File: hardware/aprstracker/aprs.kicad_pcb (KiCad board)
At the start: 2 copper layers, 125 parts, among them IC1 ATMEGA8-AI, J1 SMA, J2 SMA, P1 CONN_6, P3 CONN_2, Q1 MMBT5551, Q2 MMBT5551, Q3 BCX54, Q4 BFR93A, Q5 BFR93A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

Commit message: [HW] Add uncommited changes / PCB updates
Signed-off-by: Angel Hitov <angelhitov@gmail.com>
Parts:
- removed C20, C48: C, SM0805
- removed C36, C45, C47, C49: CAPAPOL, c_elec_6.3x4.5
- added ASTUB: VAL**, ASTUB, F.Cu at (164.7, 85.9)
- added D8: LED, LED-0805, F.Cu at (184.7, 90.3)
- added R30: R, SM0805, F.Cu at (188.1, 89.3)
- moved C43 77.2 mm to (109.0, 102.0), turned to 270 degrees
- moved R24 56.2 mm to (149.4, 94.2), turned to 270 degrees
- moved C1 53.8 mm to (133.7, 109.7)
- moved C50 53.1 mm to (184.8, 118.6), turned to 0 degrees
- moved C51 51.9 mm to (172.3, 116.2), turned to 0 degrees
- moved C22 50.5 mm to (153.0, 94.6), turned to 180 degrees
- moved C23 49.3 mm to (151.6, 86.7), turned to 180 degrees
- moved C18 48.8 mm to (157.6, 90.9), turned to 90 degrees
- moved D1 48.8 mm to (161.3, 100.2)
- moved C11 48.7 mm to (166.1, 111.9)
- moved C12 48.7 mm to (162.6, 111.9)
- moved C15 48.7 mm to (161.3, 97.5)
- moved C17 48.7 mm to (159.8, 90.9)
- moved C21 48.7 mm to (132.8, 95.2)
- moved C29 48.7 mm to (100.8, 105.7)
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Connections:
- C1 pad 2: N-0000089 (its old number) -> N-0000090
- C23 pad 1: N-0000060 (its old number) -> N-0000059
- C24 pad 1: N-0000060 (its old number) -> N-0000059
- C4 pad 2: N-0000022 -> N-0000019
- C5 pad 2: N-0000021 -> N-0000022
- IC1 pad 7: N-0000022 -> N-0000019
- IC1 pad 8: N-0000021 -> N-0000022
- L7 pad 2: N-0000060 (its old number) -> N-0000059
- Q5 pad 2: N-0000082 (its old number) -> N-0000043
- Q5 pad 3: N-0000060 (its old number) -> N-0000059
- R24 pad 1: N-0000082 (its old number) -> N-0000059
- R26 pad 1: N-0000082 (its old number) -> N-0000043
- U1 pad 2: N-0000089 (its old number) -> N-0000090
- X1 pad 1: N-0000089 (its old number) -> N-0000013
- X1 pad 2: N-0000013 -> N-0000090
- X2 pad 1: N-0000021 -> N-0000019
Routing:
- net VCC: track 0.00 -> 98.5 mm
- net TXD: track 0.00 -> 81.1 mm
- net RXD: track 0.00 -> 66.4 mm
- net N-0000034: track 0.00 -> 42.6 mm
- net N-0000068: track 0.00 -> 24.3 mm
- net N-0000094: track 0.00 -> 23.0 mm
- net RF_EN: track 0.00 -> 20.3 mm
- net N-0000011: track 0.00 -> 18.0 mm
- net N-0000022: track 0.00 -> 16.2 mm
- net N-0000019: track 0.00 -> 14.7 mm
- net N-0000059: track 0.00 -> 14.2 mm
- net N-0000025: track 0.00 -> 13.2 mm
- net N-0000044: track 0.00 -> 11.1 mm
- net N-0000027: track 0.00 -> 10.8 mm
- net N-0000024: track 0.00 -> 10.8 mm
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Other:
- board outline added: 102 x 38 mm

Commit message: [HW] route pcb
Signed-off-by: Angel Hitov <angelhitov@gmail.com>
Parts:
- moved R14 47.4 mm to (108.8, 96.9), turned to 90 degrees
- moved L16 46.8 mm to (162.7, 118.1)
- moved C32 12.3 mm to (121.3, 83.3), turned to 180 degrees
- moved D4 5.23 mm to (125.2, 102.6), turned to 0 degrees
- moved Q2 3.24 mm to (107.2, 92.6), turned to 90 degrees
- moved C38 2.17 mm to (116.8, 102.1)
- moved C21 1.48 mm to (133.6, 94.0), turned to 180 degrees
- moved R16 1.02 mm to (126.4, 110.9)
- moved L3 0.89 mm to (128.8, 107.1)
- moved R27 0.51 mm to (101.0, 99.3)
- moved Q7 0.51 mm to (101.0, 96.4)
- moved R29 0.38 mm to (101.3, 93.3)
- moved R28 0.25 mm to (98.2, 100.6)
- moved R9 0.25 mm to (152.7, 104.3)
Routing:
- net GND: track 6.69 -> 266.8 mm, vias 0 -> 70
- net VDD: track 7.79 -> 113.1 mm, vias 0 -> 3
- net +5V: track 6.26 -> 86.3 mm, vias 0 -> 1
- net DATA: track 0.00 -> 76.9 mm, vias 0 -> 1
- net CL: track 0.00 -> 72.5 mm, vias 0 -> 1
- net N-0000029: track 0.00 -> 72.2 mm, vias 0 -> 2
- net CE: track 0.00 -> 71.7 mm, vias 0 -> 2
- net RF_PWR: track 0.00 -> 67.4 mm, vias 0 -> 2
- net 3V3: track 0.00 -> 57.9 mm, vias 0 -> 2
- net N-0000094: track 23.0 -> 56.3 mm, vias 0 -> 3
- net N-000002: track 0.00 -> 22.4 mm
- net N-0000044: track 11.1 -> 31.3 mm, vias 0 -> 2
- net N-0000091: track 0.00 -> 20.0 mm
- net N-0000064: track 0.00 -> 18.8 mm
- net N-0000067: track 0.00 -> 14.7 mm
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- added copper zone on B.Cu, net GND
- added copper zone on F.Cu, net GND
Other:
- rule via_min_drill: 0.508 -> 0.4
- rule via_min_size: 0.889 -> 0.8

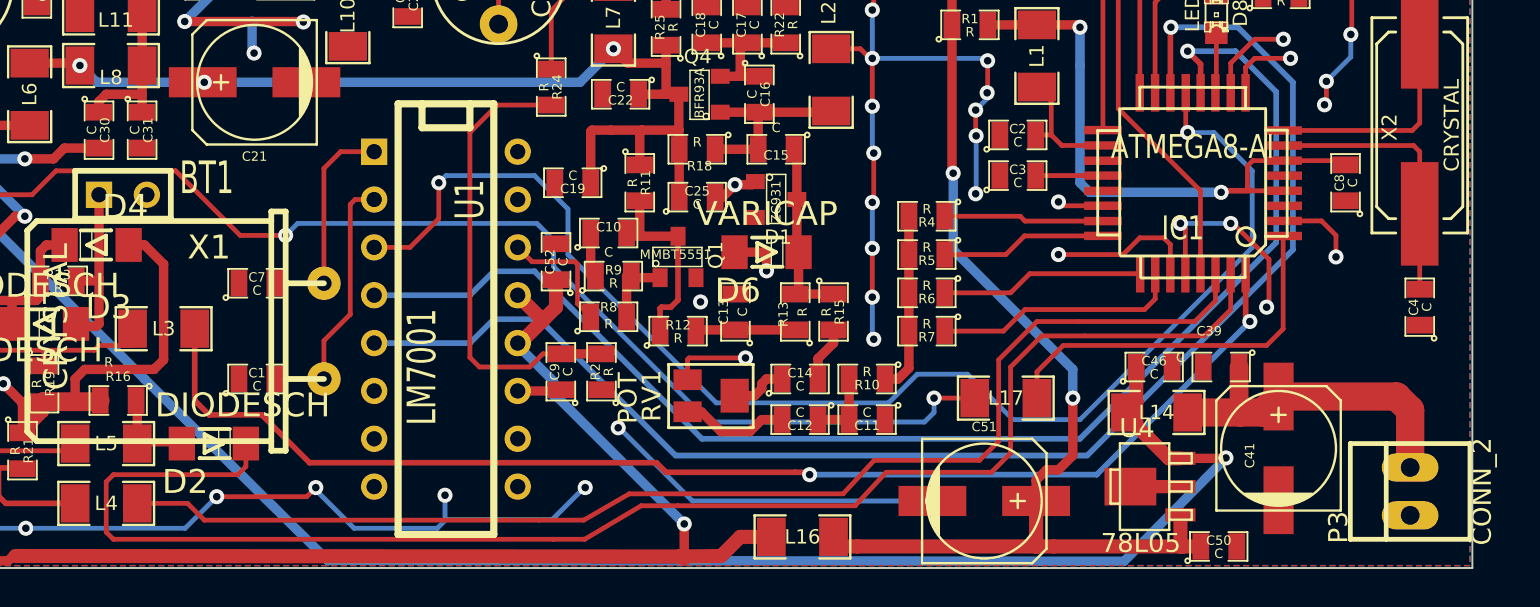
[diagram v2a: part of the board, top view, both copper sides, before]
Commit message: [HW] PCB Ground plane update
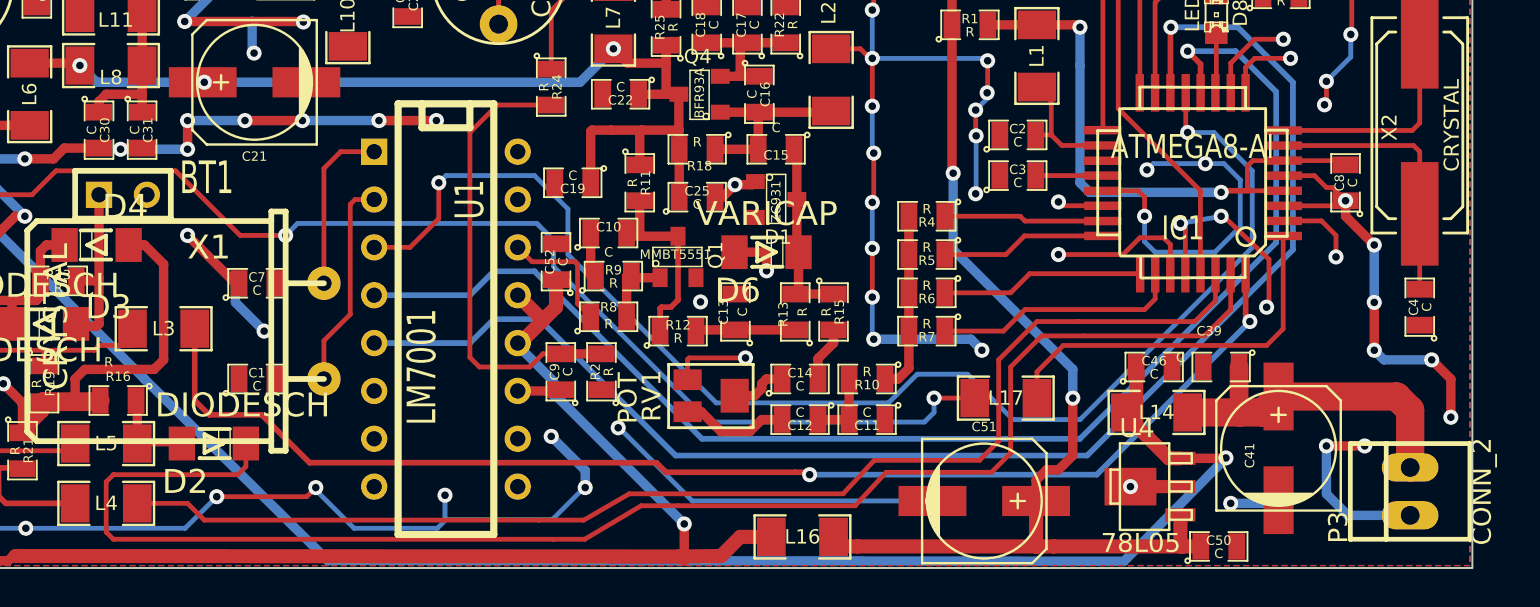
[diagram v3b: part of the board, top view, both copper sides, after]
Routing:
- net GND: track 266.8 -> 356.3 mm, vias 70 -> 94

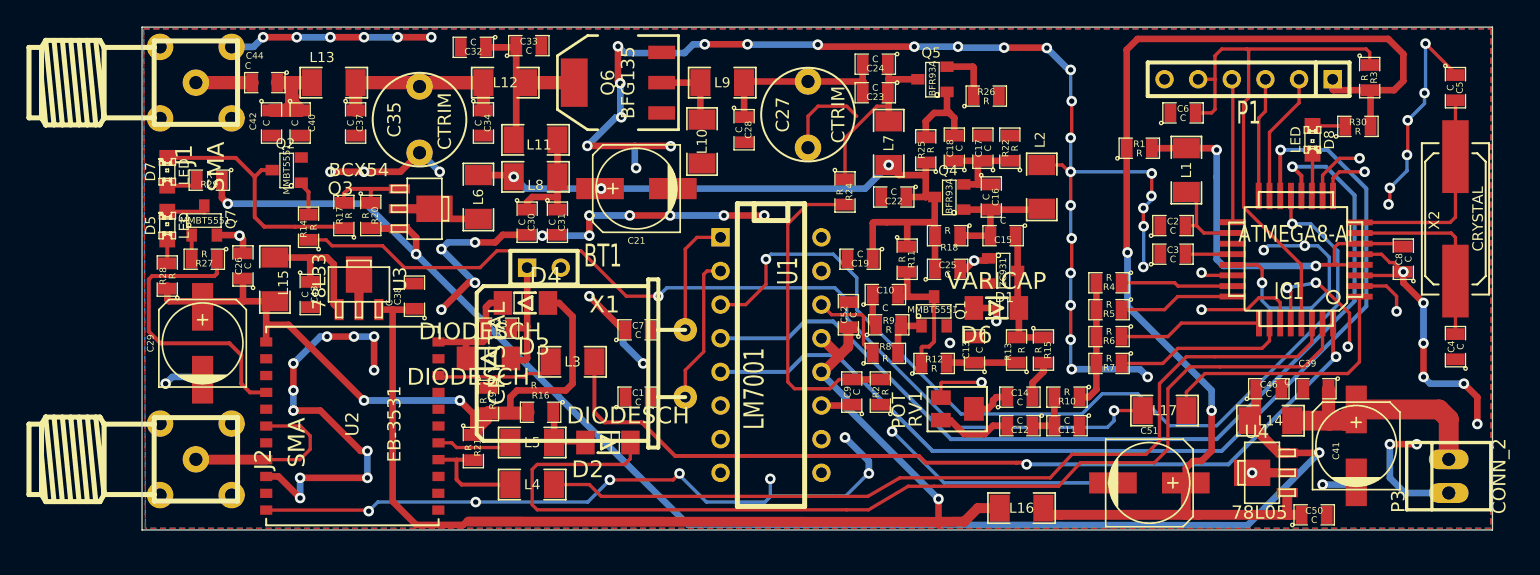
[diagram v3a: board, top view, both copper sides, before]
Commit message: [HW] Fix GPS footprint and pcb
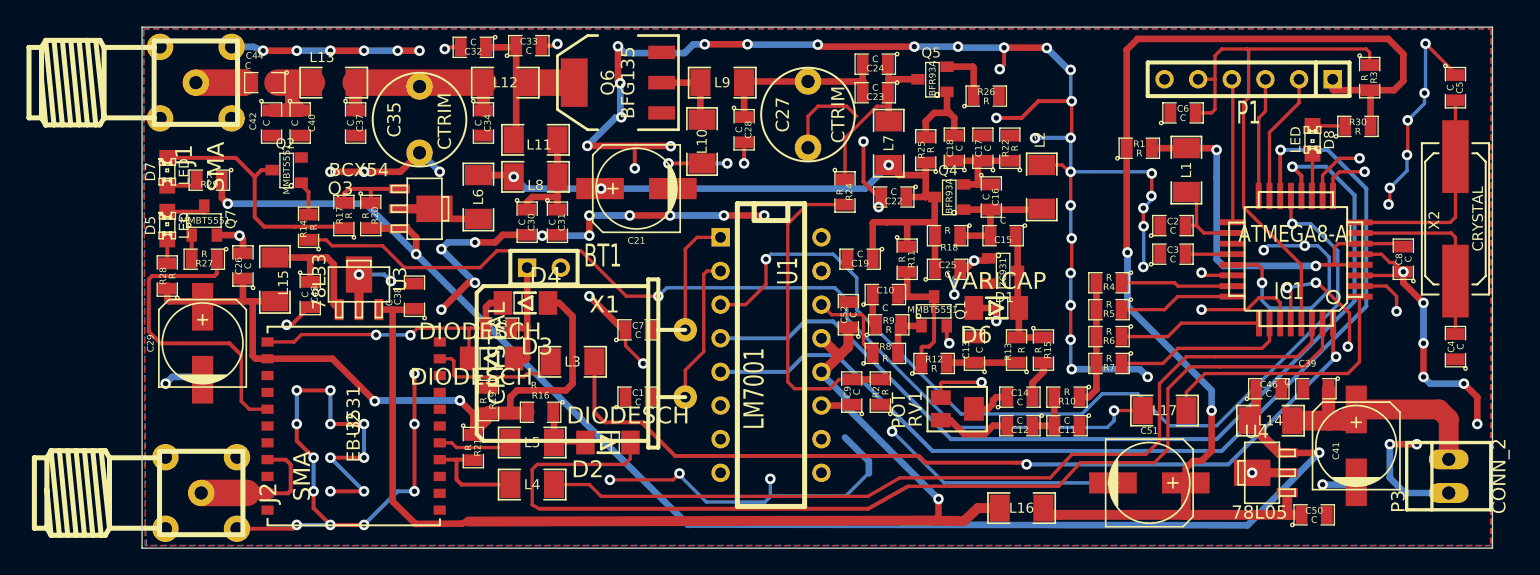
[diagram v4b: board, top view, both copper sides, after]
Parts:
- moved J2 2.57 mm to (100.7, 117.0)
- moved D3 0.23 mm to (122.7, 106.8)
- moved U2 0.10 mm to (112.2, 111.8)
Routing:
- net (no net): track 4.49 -> 33.6 mm, vias 3 -> 6
- net N-000007: track 8.83 -> 22.3 mm, vias 0 -> 2
- net N-0000066: track 4.25 -> 7.92 mm
- net N-0000076: track 13.6 -> 10.7 mm
- net N-000009: track 8.36 -> 11.0 mm
- net N-000002: track 22.4 -> 23.8 mm
- net N-0000091: track 20.0 -> 18.8 mm
- net N-000004: track 9.45 -> 10.6 mm
- net 3V3: track 57.9 -> 58.7 mm
- net GND: track 356.3 -> 355.8 mm, vias 94 -> 107
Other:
- board size 102 x 38 mm -> 102 x 39.3 mm
- board text added: "FR4 1.55mm"

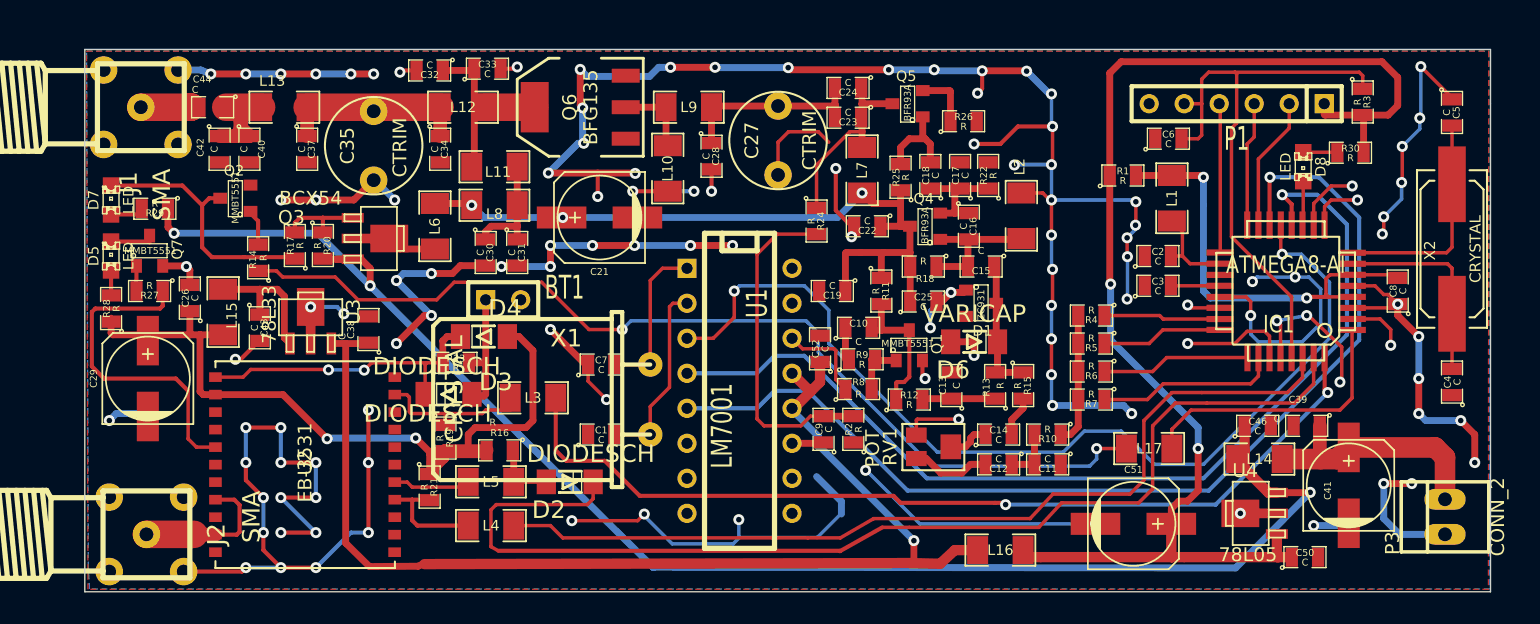
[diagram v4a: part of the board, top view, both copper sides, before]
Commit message: [HW] PCB - rearrange designators
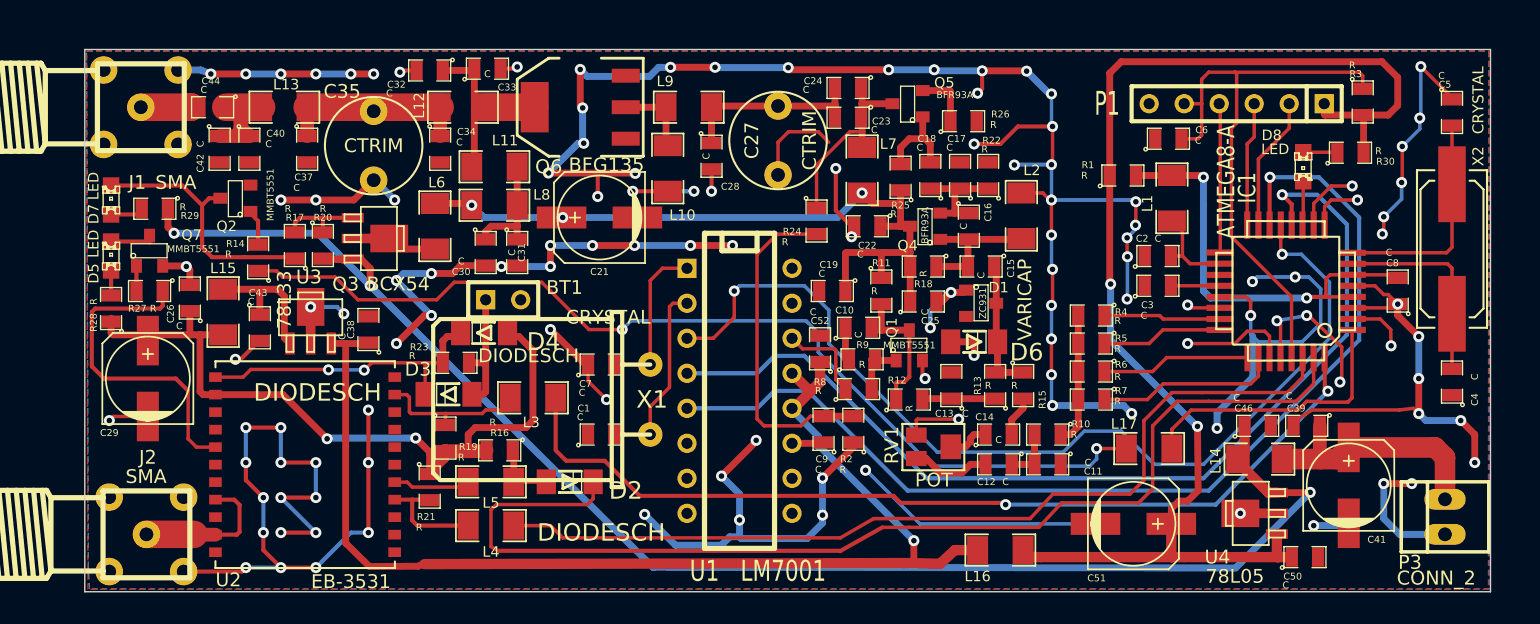
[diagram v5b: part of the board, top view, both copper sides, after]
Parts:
- moved ASTUB 55.2 mm to (109.8, 80.2)
- moved D4 0.27 mm to (125.2, 102.3)
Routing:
- net GND: track 355.8 -> 406.5 mm, vias 107 -> 116
- net (no net): track 33.6 -> 4.45 mm, vias 6 -> 2
- net N-0000085: track 9.57 -> 13.6 mm
- net N-0000059: track 14.2 -> 16.4 mm
- net N-0000015: track 5.30 -> 7.42 mm
- net N-000003: track 1.82 -> 3.64 mm
- net N-000007: track 22.3 -> 23.2 mm

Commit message: [HW] PCB - minor adjustments
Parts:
- moved R26 2.16 mm to (160.1, 84.8)
- moved J2 0.41 mm to (100.3, 117.0)
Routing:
- net GND: track 406.5 -> 611.6 mm, vias 116 -> 173
- net VCC: track 93.7 -> 83.8 mm, vias 2 -> 3
- net N-0000043: track 4.20 -> 2.04 mm
- net (no net): track 4.45 -> 2.81 mm, vias 2 -> 1
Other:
- board text added: "LZ1ARM"
